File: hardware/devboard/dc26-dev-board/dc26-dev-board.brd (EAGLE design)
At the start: 160 x 100 mm, 88 parts, among them CN1 JST, IC1 STM32F411RET6, M10 STM32-Breakout-2, U1 ESP-WROOM-32, Y1 ABL-8.000MHZ-B2

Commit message: first auto route
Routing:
- net GND: track 0.00 -> 776.6 mm, vias 0 -> 8
- net VCC: track 0.00 -> 437.6 mm, vias 0 -> 7
- net VCC1: track 0.00 -> 334.5 mm, vias 0 -> 6
- net LCD_RESET: track 0.00 -> 187.7 mm, vias 0 -> 5
- net LCD_BACKLIGHT: track 0.00 -> 167.4 mm, vias 0 -> 2
- net ESP_CS: track 0.00 -> 166.9 mm, vias 0 -> 4
- net SPI2_LCD_SCK: track 0.00 -> 129.0 mm, vias 0 -> 4
- net SPI3_ESP_SCK: track 0.00 -> 125.4 mm, vias 0 -> 4
- net PC13: track 0.00 -> 111.7 mm, vias 0 -> 4
- net PA15: track 0.00 -> 111.3 mm, vias 0 -> 4
- net SPI2_LCD_MOSI: track 0.00 -> 107.4 mm, vias 0 -> 3
- net SPI3_ESP_MOSI: track 0.00 -> 107.4 mm, vias 0 -> 1
- net LCD_CS: track 0.00 -> 104.1 mm
- net PB9: track 0.00 -> 102.5 mm, vias 0 -> 2
- net USART1_RX: track 0.00 -> 101.8 mm, vias 0 -> 4
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
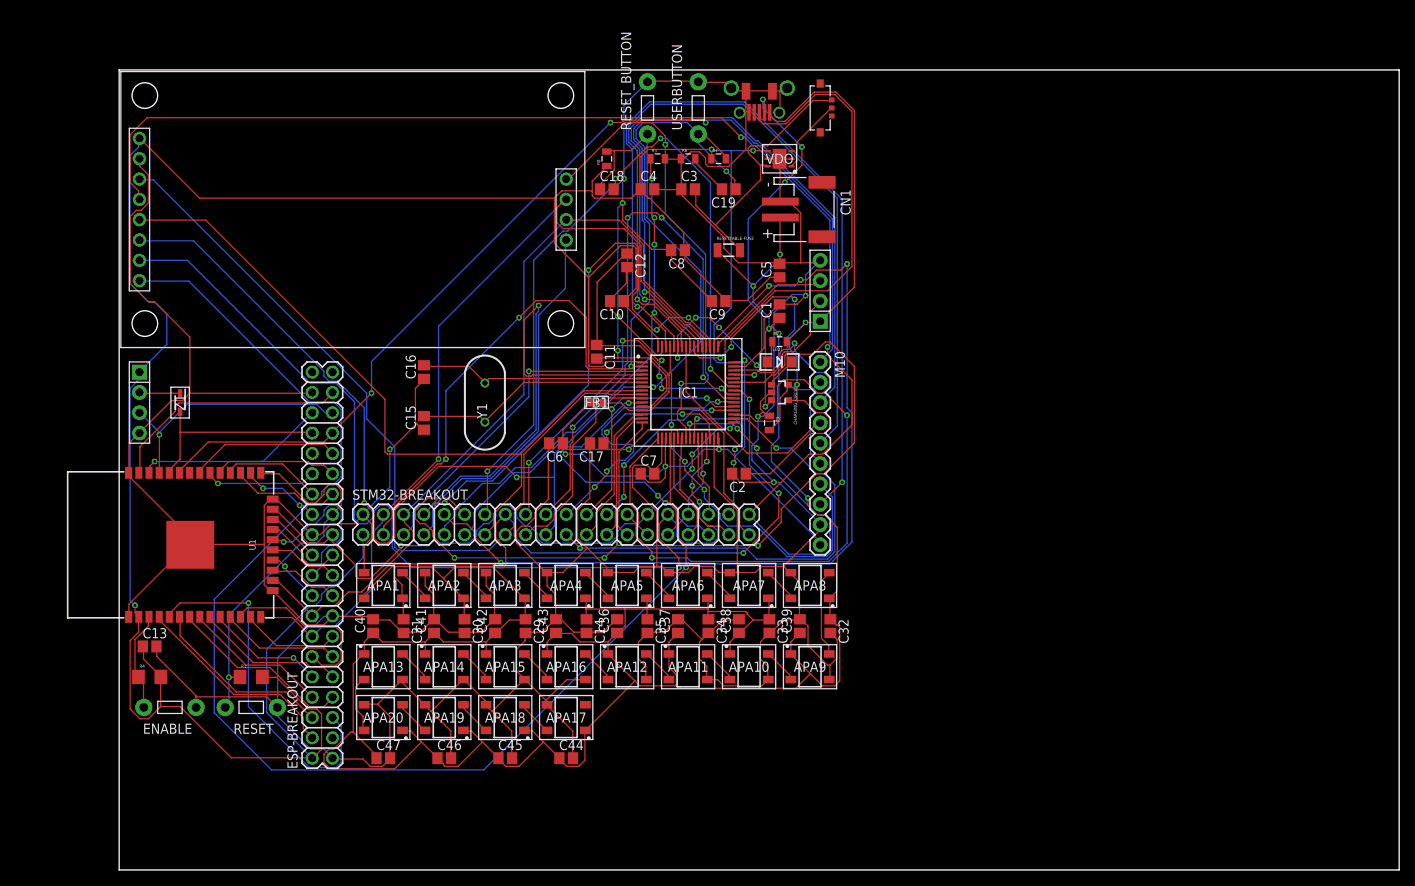
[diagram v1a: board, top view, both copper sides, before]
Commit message: auto routed boardwith some minor vcc changes by hand.
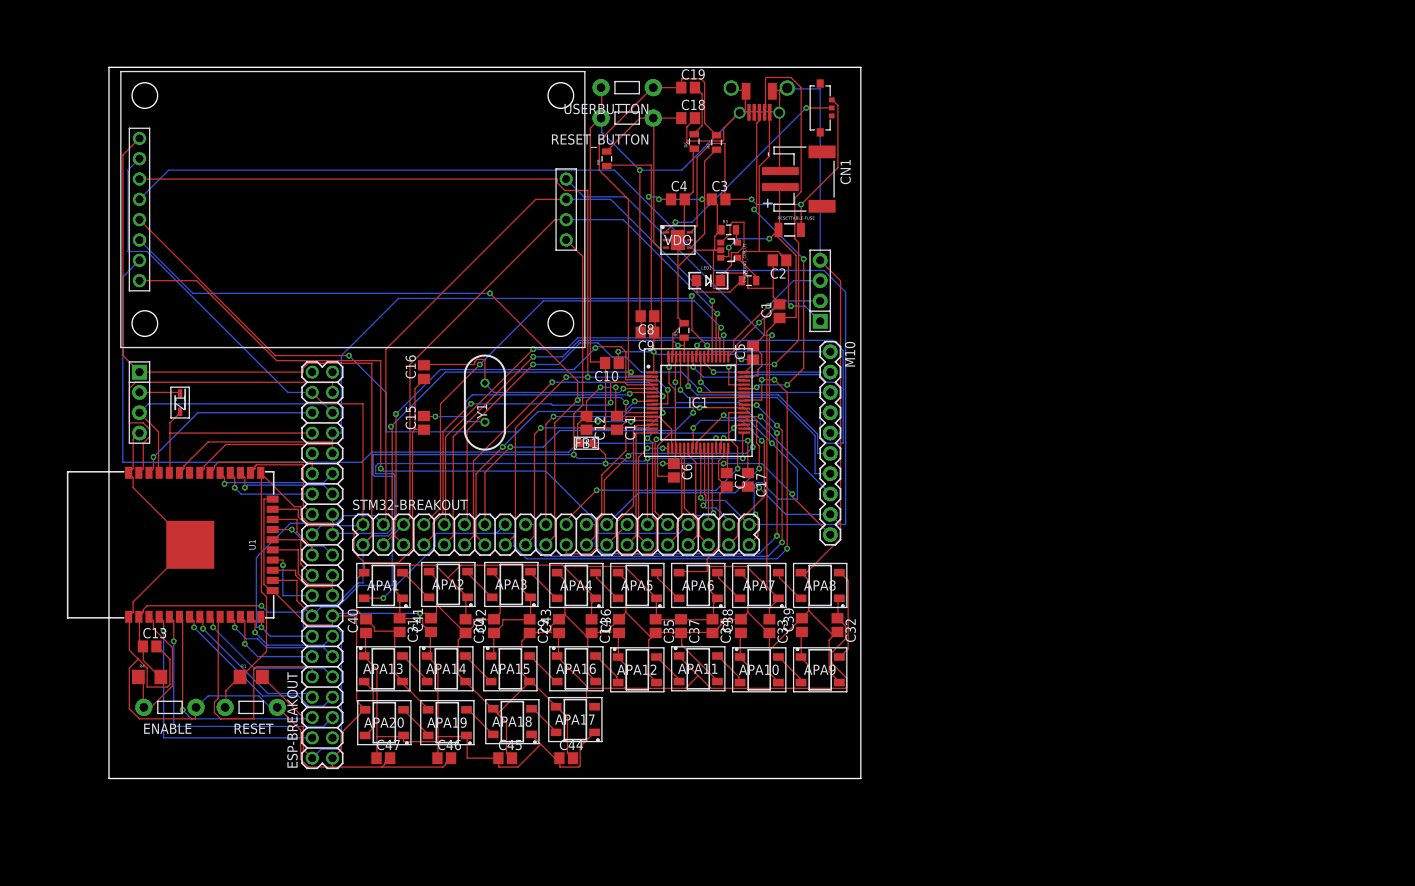
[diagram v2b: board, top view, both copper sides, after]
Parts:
- added U$2: CMD_C0DE_LOGO, dc-26:CMD_C0DE_LOGO
- added U$3: DARKNET_DD, dc-26:DARKNET_D
- added U$4: DARKNET_NN, dc-26:DARKNET_N
- added U$6: KRUX_LOGO, dc-26:KRUX_LOGO
- moved C2 27.1 mm to (82.5, 76.2)
- moved R3 24.7 mm to (76.2, 80.0), turned to 0 degrees
- moved R5 21.7 mm to (70.6, 67.4), turned to 90 degrees
- moved C12 20.9 mm to (58.4, 55.9)
- moved C17 19.5 mm to (78.6, 48.8), turned to 270 degrees
- moved CHARGING_CIRCUT 18.9 mm to (76.2, 77.5)
- moved VDO 16.3 mm to (69.8, 78.7), turned to 0 degrees
- moved C6 15.1 mm to (69.3, 49.9), turned to 270 degrees
- moved C19 13.7 mm to (71.1, 97.8), turned to 0 degrees
- moved C18 13.5 mm to (71.1, 94.0)
- moved LED1 13.5 mm to (73.7, 73.7)
- moved C5 10.8 mm to (79.2, 64.6)
- moved C7 9.94 mm to (75.9, 48.8), turned to 270 degrees
- moved C9 9.72 mm to (66.0, 67.2)
- moved USERBUTTON 9.25 mm to (63.5, 97.8), turned to 180 degrees
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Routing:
- net VCC: track 437.6 -> 341.7 mm, vias 7 -> 12
- net PB9: track 102.5 -> 29.9 mm, vias 2 -> 1
- net PB6: track 94.7 -> 28.0 mm
- net PB4: track 86.0 -> 20.0 mm
- net LCD_BACKLIGHT: track 167.4 -> 102.7 mm
- net ESP_CS: track 166.9 -> 103.9 mm, vias 4 -> 2
- net PA15: track 111.3 -> 53.7 mm, vias 4 -> 2
- net USART1_TX: track 92.5 -> 44.0 mm, vias 4 -> 2
- net USART1_RX: track 101.8 -> 53.8 mm, vias 4 -> 2
- net VCC0: track 78.2 -> 39.7 mm, vias 2 -> 1
- net LCD_RESET: track 187.7 -> 150.8 mm, vias 5 -> 1
- net PC8: track 73.1 -> 38.3 mm, vias 4 -> 2
- net PB14: track 69.1 -> 36.4 mm
- net GND: track 776.6 -> 808.7 mm, vias 8 -> 3
- net PA6: track 40.3 -> 13.1 mm, vias 3 -> 0
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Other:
- board size 160 x 100 mm -> 94 x 88.9 mm

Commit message: minor fixed of part naming and added todo file
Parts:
- P1: value SWITCH_SPDT -> SSSS811101
- renumbered U$5 to P1
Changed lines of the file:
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@@
 <element name="USB" library="dc-26" package="DX4R005JJ2" value="DX4R005JJ2DX4R005JJ2" x="80.01" y="93.98" rot="R90"/>
 <element name="LINK1" library="dc-26" package="1X04" value="STLINK-V2-CONNECTOR" x="87.63" y="73.66" rot="R90"/>
-<element name="U$5" library="dc-26" package="SPDT_SSAJ120100" value="SWITCH_SPDT" x="87.63" y="95.25" rot="R270"/>
+<element name="P1" library="dc-26" package="SPDT_SSAJ120100" value="SSSS811101" x="87.63" y="95.25" rot="R270"/>
 <element name="U1" library="dc-26" package="ESP-WROOM-32" value="ESP-WROOM-32" x="8.89" y="40.64" rot="R180"/>
 <element name="USERBUTTON" library="dc-26" package="TACTILE-2PIN-NARROW" value="UserButton" x="63.5" y="97.79" rot="R180"/>
@@
 <contactref element="C3" pad="2"/>
 <contactref element="RESETTABLE-FUSE" pad="2"/>
-<contactref element="U$5" pad="1"/>
+<contactref element="P1" pad="1"/>
 <contactref element="VDO" pad="6"/>
 <wire x1="72.23125" y1="80.48625" x2="71.4375" y2="79.6925" width="0.1524" layer="1"/>
@@
 </signal>
 <signal name="VIN-EN">
-<contactref element="U$5" pad="C"/>
+<contactref element="P1" pad="C"/>
 <contactref element="VDO" pad="1"/>
 <wire x1="85.88375" y1="95.25" x2="89.08" y2="95.25" width="0.1524" layer="1"/>

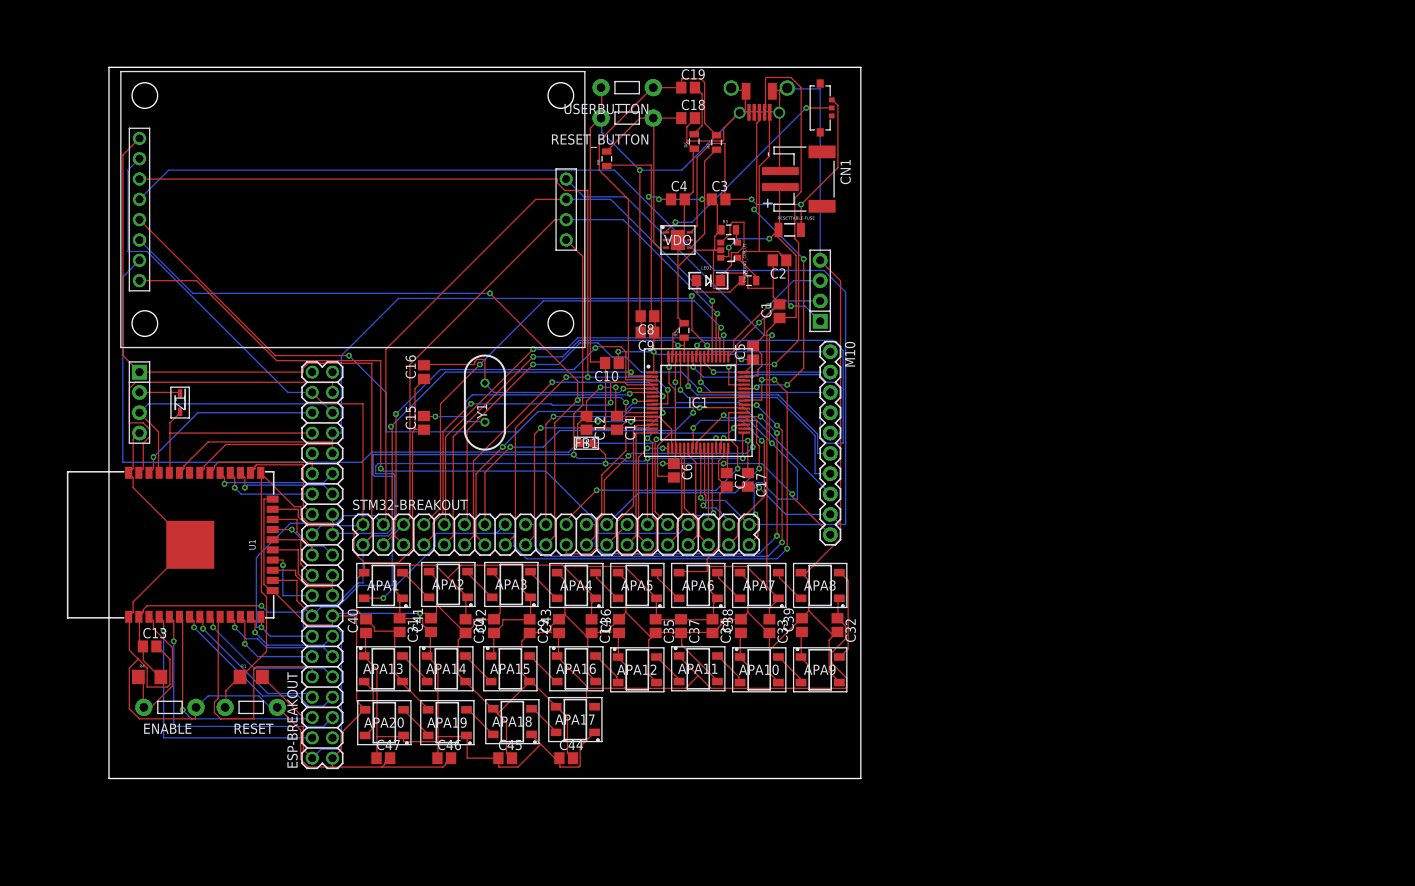
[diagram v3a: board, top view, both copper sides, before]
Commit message: added R9 to crystal moved logo and DN to tslik and bsilk layers
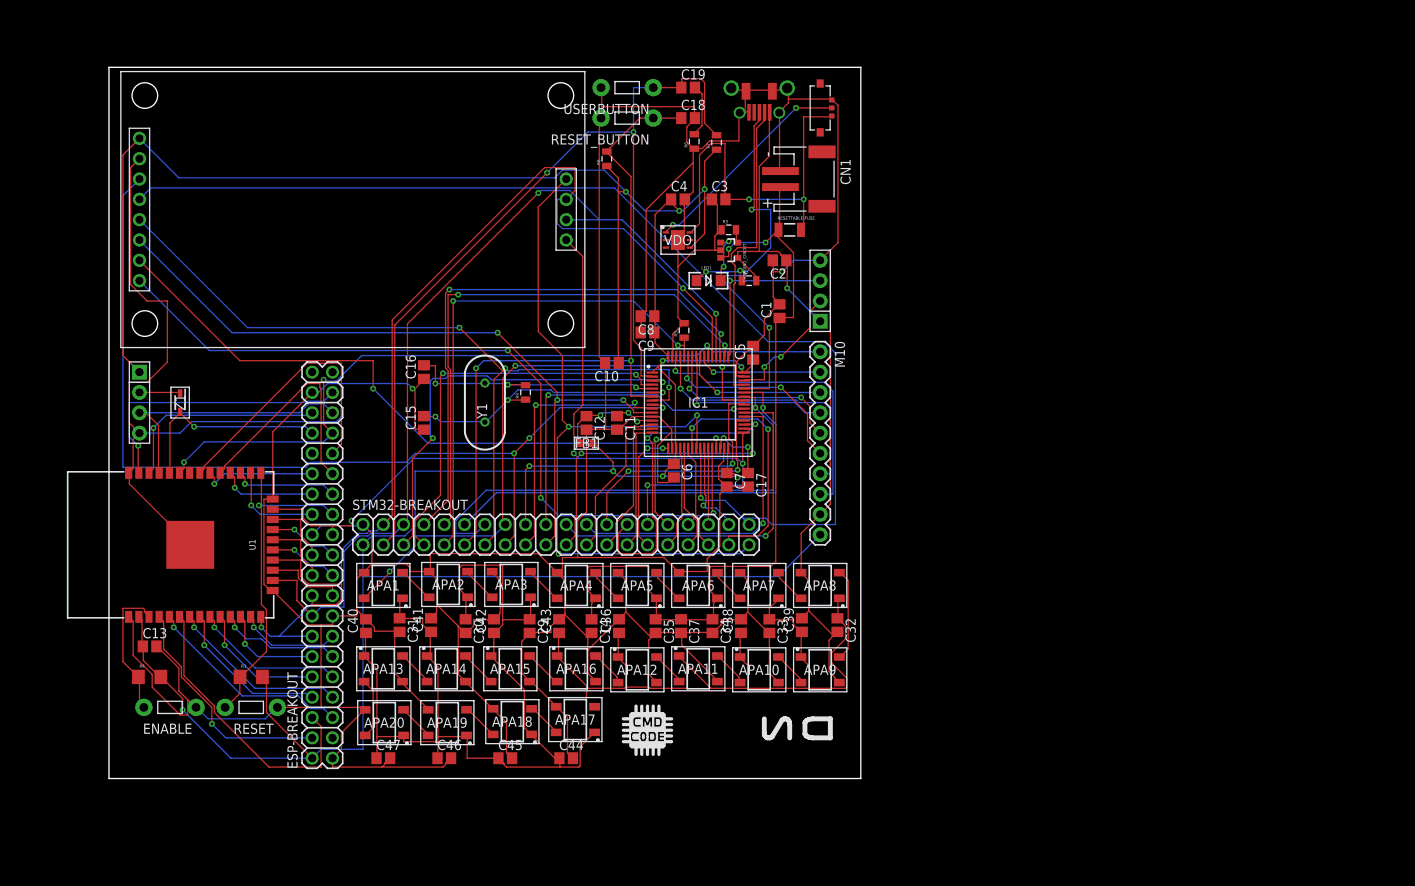
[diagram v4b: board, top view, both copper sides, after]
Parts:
- removed U$6: KRUX_LOGO, dc-26:KRUX_LOGO
- added R9: 1M, dc-26:0805
- moved U$3 9.25 mm to (88.9, 16.5), flipped to the bottom
- moved U$2 4.02 mm to (66.0, 17.8)
- moved U$4 3.59 mm to (83.8, 16.5), flipped to the bottom
- moved M10 1.27 mm to (87.6, 64.8)
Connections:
- net GND: now also P1.1
- net OSC_IN: now also R9.2
- net OSC_OUT: now also R9.1
- net VIN: now also P1.2; no longer P1.1
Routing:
- net VCC: track 341.7 -> 403.8 mm, vias 12 -> 9
- net SPI2_LCD_SCK: track 114.1 -> 96.5 mm, vias 2 -> 3
- net PB5: track 39.5 -> 22.2 mm
- net USB_DP: track 55.8 -> 38.7 mm, vias 2 -> 0
- net USART1_TX: track 44.0 -> 60.9 mm, vias 2 -> 1
- net PC13: track 106.8 -> 123.2 mm
- net IO25: track 32.4 -> 16.4 mm, vias 0 -> 1
- net IO19: track 19.3 -> 35.3 mm
- net PA15: track 53.7 -> 67.9 mm
- net BOOT0: track 50.5 -> 64.5 mm
- net GPIO_APA104_DATA: track 89.6 -> 75.8 mm, vias 4 -> 3
- net IO5: track 15.6 -> 29.2 mm, vias 1 -> 0
- net PC9: track 56.1 -> 42.7 mm, vias 3 -> 2
- net SD_CS: track 83.5 -> 95.6 mm, vias 4 -> 3
- net PC7: track 34.0 -> 44.9 mm, vias 2 -> 1
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
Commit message: more updates see last sheet for details
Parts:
- removed Z1: CMDZ3L3_TR, dc-26:SOD2512X110N
- added D1: (no value), dc-26:SOD-323
- CN1: device dc-26:JST-PH-2-SMT-RA -> dc-26:JST-PH-2-THM-RA
- R1, R4: device dc-26:1206 -> dc-26:0805
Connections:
- net ESP-RX: now also D1.1; no longer Z1.1
- net ESP-RX0: now also D1.2; no longer Z1.2
- net VCC: no longer ESP32PH.VCC
- net VCC0: no longer LINK1.VCC
- net VIN: now also ESP32PH.VCC, LINK1.VCC
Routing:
- net VCC0: track 38.7 -> 32.9 mm
- net VCC1: track 329.2 -> 332.8 mm
- net GND: track 806.3 -> 810.0 mm
- net VCC: track 403.8 -> 402.1 mm
- net ESP-EN: track 17.5 -> 18.2 mm
- net ESP-IO0: track 41.9 -> 42.6 mm
